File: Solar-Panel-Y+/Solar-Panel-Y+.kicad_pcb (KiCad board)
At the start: 6 copper layers, 50 x 50 mm, 81 parts, among them J1 FTS-105-01-L-DV-A, Q1 BSS138DWQ-7, Q2 MBT2222ADW1T1, Q3 BSS138DWQ-7, Q4 MBT2222ADW1T1, U1 Value, U2 TSL2561

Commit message: Re-distribute buses between layers
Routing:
- net COIL_N: track 32.1 -> 31.1 mm
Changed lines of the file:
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@@
   (via (at 115.8 74.1) (size 0.6) (drill 0.3) (layers "F.Cu" "B.Cu") (net 3))
   (via (at 110.249995 49.829999) (size 0.6) (drill 0.3) (layers "F.Cu" "B.Cu") (net 3))
-  (segment (start 112.297995 59.247995) (end 115.799997 62.749997) (width 0.381) (layer "In4.Cu") (net 3))
-  (segment (start 115.799997 62.749997) (end 115.799997 74.100004) (width 0.381) (layer "In4.Cu") (net 3))
-  (segment (start 110.25 49.829999) (end 112.297995 51.877994) (width 0.381) (layer "In4.Cu") (net 3))
-  (segment (start 112.297995 51.877994) (end 112.297995 59.247995) (width 0.381) (layer "In4.Cu") (net 3))
+  (segment (start 112.55 59.5) (end 115.799997 62.749997) (width 0.381) (layer "In2.Cu") (net 3))
+  (segment (start 115.799997 62.749997) (end 115.799997 74.100004) (width 0.381) (layer "In2.Cu") (net 3))
+  (segment (start 110.25 49.829999) (end 112.55 52.129999) (width 0.381) (layer "In2.Cu") (net 3))
+  (segment (start 112.55 52.129999) (end 112.55 59.5) (width 0.381) (layer "In2.Cu") (net 3))
   (segment (start 110.25 49.829999) (end 112.297995 49.829999) (width 0.381) (layer "B.Cu") (net 3))
   (segment (start 116.828 74.5485) (end 116.2485 74.5485) (width 0.508) (layer "B.Cu") (net 3))
@@
   (via (at 119.225 74.1) (size 0.6) (drill 0.3) (layers "F.Cu" "B.Cu") (net 8))
   (via (at 118.725 49.825) (size 0.6) (drill 0.3) (layers "F.Cu" "B.Cu") (net 8))
-  (segment (start 119.225 59.775) (end 119.225 74.1) (width 0.381) (layer "In4.Cu") (net 8))
-  (segment (start 116.367995 56.917995) (end 119.225 59.775) (width 0.381) (layer "In4.Cu") (net 8))
-  (segment (start 118.725 49.825) (end 116.367995 52.182005) (width 0.381) (layer "In4.Cu") (net 8))
-  (segment (start 116.367995 52.182005) (end 116.367995 56.917995) (width 0.381) (layer "In4.Cu") (net 8))
+  (segment (start 120.4 58.6) (end 119.225 59.775) (width 0.381) (layer "In2.Cu") (net 8))
+  (segment (start 120.4 51.5) (end 120.4 58.6) (width 0.381) (layer "In2.Cu") (net 8))
+  (segment (start 119.225 59.775) (end 119.225 74.1) (width 0.381) (layer "In2.Cu") (net 8))
+  (segment (start 118.725 49.825) (end 120.4 51.5) (width 0.381) (layer "In2.Cu") (net 8))
   (segment (start 118.225 73.6) (end 118.725 73.6) (width 0.508) (layer "B.Cu") (net 8))
   (segment (start 118.725 49.825) (end 116.372994 49.825) (width 0.381) (layer "B.Cu") (net 8))
@@
   (via (at 108.9 56.9) (size 0.6) (drill 0.3) (layers "F.Cu" "B.Cu") (net 11))
   (via (at 104.6 56.9) (size 0.6) (drill 0.3) (layers "F.Cu" "B.Cu") (net 11))
-  (segment (start 104 56.9) (end 104.6 56.9) (width 0.762) (layer "In1.Cu") (net 11))
-  (segment (start 100.25 56.9) (end 104 56.9) (width 0.762) (layer "In1.Cu") (net 11))
-  (segment (start 98 56.9) (end 100.25 56.9) (width 0.762) (layer "In1.Cu") (net 11))
-  (segment (start 96.95 56.9) (end 98 56.9) (width 0.762) (layer "In1.Cu") (net 11))
-  (segment (start 104 56.9) (end 108.9 56.9) (width 0.762) (layer "In1.Cu") (net 11))
+  (segment (start 104 56.9) (end 104.6 56.9) (width 0.762) (layer "In3.Cu") (net 11))
+  (segment (start 100.25 56.9) (end 104 56.9) (width 0.762) (layer "In3.Cu") (net 11))
+  (segment (start 98 56.9) (end 100.25 56.9) (width 0.762) (layer "In3.Cu") (net 11))
+  (segment (start 96.95 56.9) (end 98 56.9) (width 0.762) (layer "In3.Cu") (net 11))
+  (segment (start 104 56.9) (end 108.9 56.9) (width 0.762) (layer "In3.Cu") (net 11))
   (segment (start 98.05 57.5) (end 98.05 58.68684) (width 0.508) (layer "B.Cu") (net 11))
   (via (at 128.1 81.2) (size 0.6) (drill 0.3) (layers "F.Cu" "B.Cu") (net 12))
@@
   (via (at 98.23692 71.57239) (size 0.6) (drill 0.3) (layers "F.Cu" "B.Cu") (net 15))
   (via (at 100.1 64.7) (size 0.6) (drill 0.3) (layers "F.Cu" "B.Cu") (net 15))
-  (segment (start 100.1 64.7) (end 98.23692 66.56308) (width 0.254) (layer "In4.Cu") (net 15))
-  (segment (start 98.23692 66.56308) (end 98.23692 71.57239) (width 0.254) (layer "In4.Cu") (net 15))
+  (segment (start 100.1 64.7) (end 98.23692 66.56308) (width 0.254) (layer "In2.Cu") (net 15))
+  (segment (start 98.23692 66.56308) (end 98.23692 71.57239) (width 0.254) (layer "In2.Cu") (net 15))
   (segment (start 99.899264 64.900736) (end 99.899264 65.48) (width 0.254) (layer "B.Cu") (net 15))
   (segment (start 100.1 64.7) (end 99.899264 64.900736) (width 0.254) (layer "B.Cu") (net 15))
@@
   (via (at 95.7 58.7) (size 0.6) (drill 0.3) (layers "F.Cu" "B.Cu") (net 21))
   (via (at 122.35 58.7) (size 0.6) (drill 0.3) (layers "F.Cu" "B.Cu") (net 21))
-  (segment (start 95.7 58.7) (end 121.2 58.7) (width 0.762) (layer "In1.Cu") (net 21))
-  (segment (start 121.2 58.7) (end 122.35 58.7) (width 0.762) (layer "In1.Cu") (net 21))
-  (segment (start 121.2 58.7) (end 121.55 58.7) (width 0.762) (layer "In1.Cu") (net 21))
+  (segment (start 95.7 58.7) (end 121.2 58.7) (width 0.762) (layer "In3.Cu") (net 21))
+  (segment (start 121.2 58.7) (end 122.35 58.7) (width 0.762) (layer "In3.Cu") (net 21))
   (segment (start 94.050002 58.70001) (end 95.700012 58.70001) (width 0.6096) (layer "B.Cu") (net 21))
   (via (at 111.605 69.45) (size 0.6) (drill 0.3) (layers "F.Cu" "B.Cu") (net 22))
@@
   (via (at 99.75 75.55) (size 0.6) (drill 0.3) (layers "F.Cu" "B.Cu") (net 29))
   (via (at 117.075 70.95) (size 0.6) (drill 0.3) (layers "F.Cu" "B.Cu") (net 29))
-  (segment (start 117.075 70.95) (end 112.125 70.95) (width 0.254) (layer "In1.Cu") (net 29))
-  (segment (start 99.75 74.475) (end 99.75 75.55) (width 0.254) (layer "In1.Cu") (net 29))
-  (segment (start 110.975 72.1) (end 102.125 72.1) (width 0.254) (layer "In1.Cu") (net 29))
-  (segment (start 112.125 70.95) (end 110.975 72.1) (width 0.254) (layer "In1.Cu") (net 29))
-  (segment (start 102.125 72.1) (end 99.75 74.475) (width 0.254) (layer "In1.Cu") (net 29))
+  (segment (start 117.075 70.95) (end 112.125 70.95) (width 0.254) (layer "In3.Cu") (net 29))
+  (segment (start 99.75 74.475) (end 99.75 75.55) (width 0.254) (layer "In3.Cu") (net 29))
+  (segment (start 110.975 72.1) (end 102.125 72.1) (width 0.254) (layer "In3.Cu") (net 29))
+  (segment (start 112.125 70.95) (end 110.975 72.1) (width 0.254) (layer "In3.Cu") (net 29))
+  (segment (start 102.125 72.1) (end 99.75 74.475) (width 0.254) (layer "In3.Cu") (net 29))
   (segment (start 116.275 67.275) (end 116.625 67.275) (width 0.254) (layer "B.Cu") (net 29))
   (segment (start 116.225 68.575) (end 115.925 68.275) (width 0.254) (layer "B.Cu") (net 29))
@@
   (via (at 110.58 71.2) (size 0.6) (drill 0.3) (layers "F.Cu" "B.Cu") (net 33))
   (via (at 98.875 75.55) (size 0.6) (drill 0.3) (layers "F.Cu" "B.Cu") (net 33))
-  (segment (start 98.875 74.125) (end 101.8 71.2) (width 0.254) (layer "In1.Cu") (net 33))
-  (segment (start 98.875 75.55) (end 98.875 74.125) (width 0.254) (layer "In1.Cu") (net 33))
-  (segment (start 101.8 71.2) (end 110.58 71.2) (width 0.254) (layer "In1.Cu") (net 33))
+  (segment (start 98.875 74.125) (end 101.8 71.2) (width 0.254) (layer "In3.Cu") (net 33))
+  (segment (start 98.875 75.55) (end 98.875 74.125) (width 0.254) (layer "In3.Cu") (net 33))
+  (segment (start 101.8 71.2) (end 110.58 71.2) (width 0.254) (layer "In3.Cu") (net 33))
   (segment (start 110.58 71.2) (end 109.38 71.2) (width 0.254) (layer "B.Cu") (net 33))
   (segment (start 107.9412 67.275) (end 108.375 67.275) (width 0.254) (layer "B.Cu") (net 33))
@@
   (via (at 100.1 69.05) (size 0.6) (drill 0.3) (layers "F.Cu" "B.Cu") (net 35))
   (via (at 100.875 66.475) (size 0.6) (drill 0.3) (layers "F.Cu" "B.Cu") (net 35))
-  (segment (start 100.1 69.05) (end 100.1 67.25) (width 0.254) (layer "In4.Cu") (net 35))
-  (segment (start 100.1 67.25) (end 100.875 66.475) (width 0.254) (layer "In4.Cu") (net 35))
+  (segment (start 100.1 69.05) (end 100.1 67.25) (width 0.254) (layer "In2.Cu") (net 35))
+  (segment (start 100.1 67.25) (end 100.875 66.475) (width 0.254) (layer "In2.Cu") (net 35))
   (segment (start 101.61453 66.48478) (end 102.62692 65.47239) (width 0.254) (layer "B.Cu") (net 35))
   (segment (start 100.1 69.05) (end 100.43692 69.38692) (width 0.254) (layer "B.Cu") (net 35))
@@
   (via (at 89.02792 62.17208) (size 0.6) (drill 0.3) (layers "F.Cu" "B.Cu") (net 39))
   (via (at 98.6 63.11) (size 0.6) (drill 0.3) (layers "F.Cu" "B.Cu") (net 39))
-  (segment (start 97.66208 62.17208) (end 98.6 63.11) (width 0.254) (layer "In4.Cu") (net 39))
-  (segment (start 89.02792 62.17208) (end 97.66208 62.17208) (width 0.254) (layer "In4.Cu") (net 39))
+  (segment (start 97.66208 62.17208) (end 98.6 63.11) (width 0.254) (layer "In2.Cu") (net 39))
+  (segment (start 89.02792 62.17208) (end 97.66208 62.17208) (width 0.254) (layer "In2.Cu") (net 39))
   (segment (start 89.02792 62.17208) (end 89.02792 63.17684) (width 0.254) (layer "B.Cu") (net 39))
   (segment (start 98.199264 63.510736) (end 98.199264 64.78) (width 0.29972) (layer "B.Cu") (net 39))

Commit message: Finished Y- Board
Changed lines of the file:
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@@
   (gr_line (start 129.599994 35.199993) (end 79.599993 35.199993) (layer "Edge.Cuts") (width 0.0508))
   (gr_line (start 129.599994 85.199995) (end 129.599994 35.199993) (layer "Edge.Cuts") (width 0.0508))
-  (gr_text "v04" (at 109.1 82.8) (layer "B.Cu")
-    (effects (font (size 1.016 1.016) (thickness 0.2032)) (justify mirror))
-  )
   (gr_text "+" (at 117.6 71.7 270) (layer "B.SilkS")
     (effects (font (size 1.143 1.143) (thickness 0.2032)) (justify mirror))

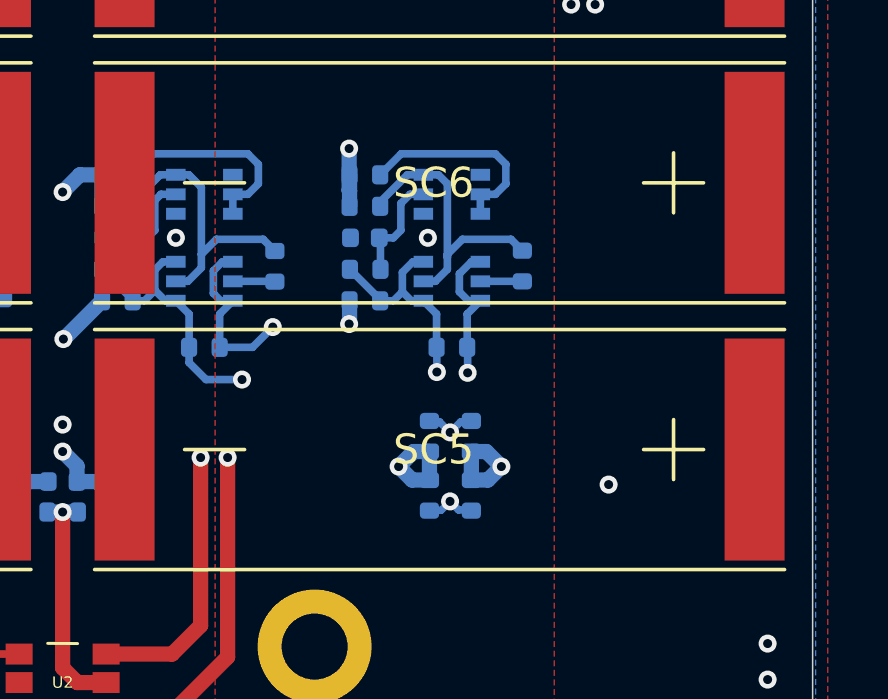
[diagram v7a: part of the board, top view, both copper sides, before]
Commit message: Modified coil resistors to allow only one to be populated
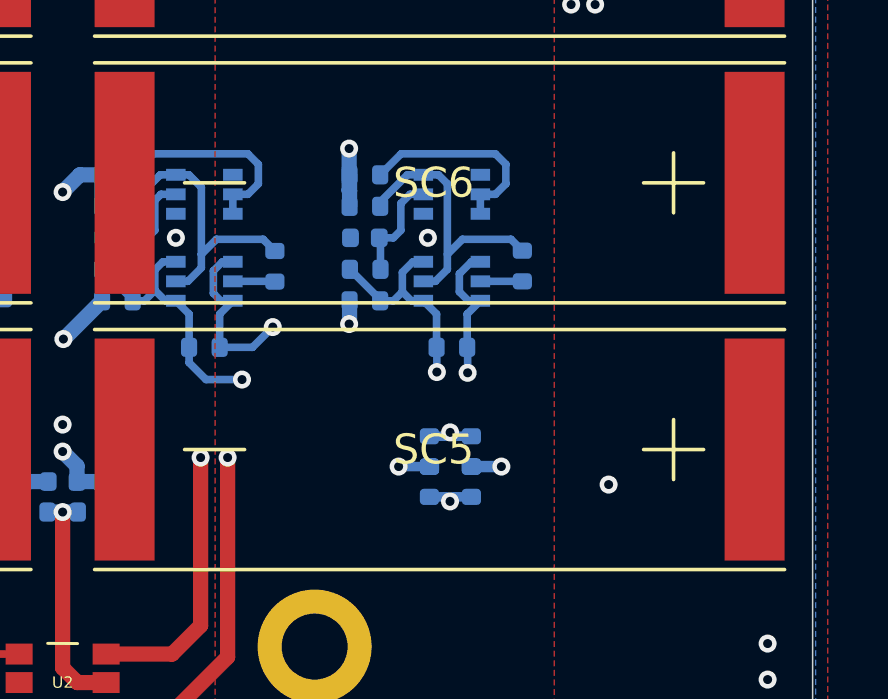
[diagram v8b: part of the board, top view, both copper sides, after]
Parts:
- moved R13 0.51 mm to (116.8, 73.6)
- moved R18 0.51 mm to (118.2, 73.6)
- moved R12 0.46 mm to (116.8, 74.6)
- moved R17 0.46 mm to (118.2, 74.6)
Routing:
- net VBAT: track 50.0 -> 44.3 mm
- net COIL_P: track 32.0 -> 29.6 mm
- net COIL_N: track 31.1 -> 28.8 mm
- net Net-(D3-Pad1): track 13.7 -> 13.1 mm
